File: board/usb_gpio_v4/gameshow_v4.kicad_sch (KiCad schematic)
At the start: 27 parts, among them J1 NC3FAAH, J2 NC3FAAH, J3 NC3FAAH, J4 NC3FAAH

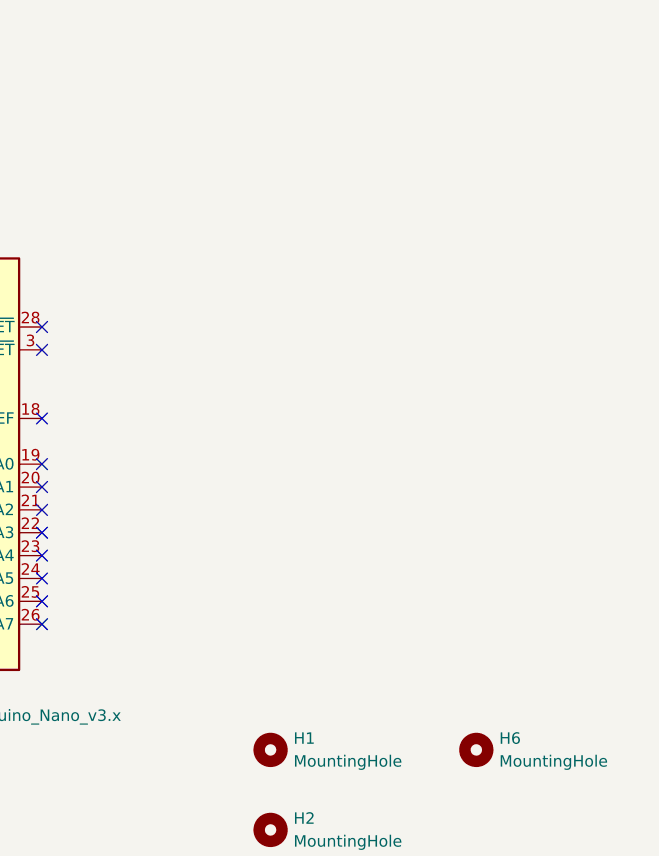
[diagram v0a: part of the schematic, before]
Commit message: add test switches
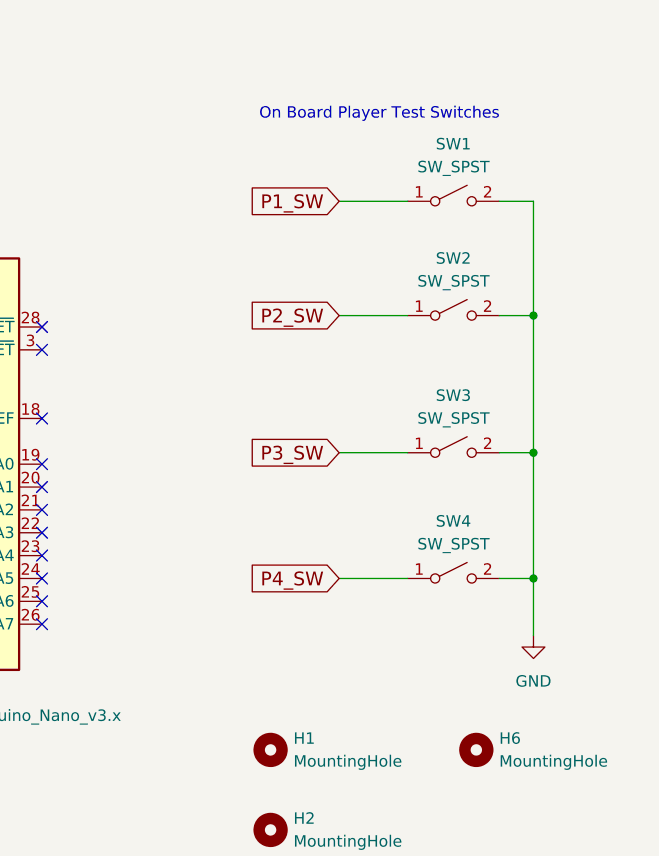
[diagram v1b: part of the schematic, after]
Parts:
- added SW1, SW2, SW3, SW4: SW_SPST, Button_Switch_SMD:SW_SPST_Omron_B3FS-101xP, symbol Switch:SW_SPST
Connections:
- net GND: now also SW1.2 (B), SW2.2 (B), SW3.2 (B), SW4.2 (B)
- net P1_SW: now also SW1.1 (A)
- net P2_SW: now also SW2.1 (A)
- net P3_SW: now also SW3.1 (A)
- net P4_SW: now also SW4.1 (A)
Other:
- note added: "On Board Player Test Switches"
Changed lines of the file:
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@@
   (junction (at 31.75 144.78) (diameter 0) (color 0 0 0 0)
   )
+  (junction (at 271.78 85.09) (diameter 0) (color 0 0 0 0)
+  )
+  (junction (at 271.78 99.06) (diameter 0) (color 0 0 0 0)
+  )
   (junction (at 127 45.72) (diameter 0) (color 0 0 0 0)
   )
@@
   )
   (junction (at 64.77 72.39) (diameter 0) (color 0 0 0 0)
+  )
+  (junction (at 271.78 69.85) (diameter 0) (color 0 0 0 0)
   )
   (junction (at 115.57 45.72) (diameter 0) (color 0 0 0 0)
@@
     (stroke (width 0) (type default))
   )
+  (wire (pts (xy 250.19 99.06) (xy 257.81 99.06))
+    (stroke (width 0) (type default))
+  )
   (wire (pts (xy 31.75 72.39) (xy 31.75 91.44))
     (stroke (width 0) (type default))
@@
     (stroke (width 0) (type default))
   )
+  (wire (pts (xy 271.78 99.06) (xy 271.78 85.09))
+    (stroke (width 0) (type default))
+  )
   (wire (pts (xy 207.01 118.11) (xy 204.47 118.11))
     (stroke (width 0) (type default))
@@
     (stroke (width 0) (type default))
   )
+  (wire (pts (xy 271.78 57.15) (xy 267.97 57.15))
+    (stroke (width 0) (type default))
+  )
   (wire (pts (xy 127 45.72) (xy 207.01 45.72))
     (stroke (width 0) (type default))
@@
     (stroke (width 0) (type default))
   )
+  (wire (pts (xy 267.97 85.09) (xy 271.78 85.09))
+    (stroke (width 0) (type default))
+  )
   (wire (pts (xy 31.75 144.78) (xy 31.75 158.75))
     (stroke (width 0) (type default))
@@
     (stroke (width 0) (type default))
   )
+  (wire (pts (xy 267.97 99.06) (xy 271.78 99.06))
+    (stroke (width 0) (type default))
+  )
   (wire (pts (xy 176.53 101.6) (xy 176.53 100.33))
     (stroke (width 0) (type default))
@@
     (stroke (width 0) (type default))
   )
+  (wire (pts (xy 271.78 85.09) (xy 271.78 69.85))
+    (stroke (width 0) (type default))
+  )
   (wire (pts (xy 69.85 102.87) (xy 63.5 102.87))
     (stroke (width 0) (type default))
@@
     (stroke (width 0) (type default))
   )
+  (wire (pts (xy 250.19 57.15) (xy 257.81 57.15))
+    (stroke (width 0) (type default))
+  )
   (wire (pts (xy 69.85 162.56) (xy 64.77 162.56))
     (stroke (width 0) (type default))
@@
     (stroke (width 0) (type default))
   )
+  (wire (pts (xy 271.78 69.85) (xy 271.78 57.15))
+    (stroke (width 0) (type default))
+  )
   (wire (pts (xy 31.75 158.75) (xy 31.75 179.07))
     (stroke (width 0) (type default))
@@
     (stroke (width 0) (type default))
   )
+  (wire (pts (xy 250.19 85.09) (xy 257.81 85.09))
+    (stroke (width 0) (type default))
+  )
+  (wire (pts (xy 271.78 105.41) (xy 271.78 99.06))
+    (stroke (width 0) (type default))
+  )
+  (wire (pts (xy 250.19 69.85) (xy 257.81 69.85))
+    (stroke (width 0) (type default))
+  )
   (wire (pts (xy 69.85 130.81) (xy 63.5 130.81))
     (stroke (width 0) (type default))
@@
     (stroke (width 0) (type default))
   )
+  (wire (pts (xy 267.97 69.85) (xy 271.78 69.85))
+    (stroke (width 0) (type default))
+  )
   (wire (pts (xy 167.64 86.36) (xy 191.77 86.36))
     (stroke (width 0) (type default))
@@
   (wire (pts (xy 48.26 91.44) (xy 43.18 91.44))
     (stroke (width 0) (type default))
+  )
+  (text "On Board Player Test Switches" (at 241.3 48.26 0)
+    (effects (font (size 1.27 1.27)) (justify left bottom))
   )
   (text "11/10/2023" (at 207.01 194.31 0)
@@
     )
   )
+  (global_label "P4_SW" (shape input) (at 250.19 99.06 180)
+    (effects (font (size 1.524 1.524)) (justify right))
+    (property "Intersheetrefs" "${INTERSHEET_REFS}" (at 250.19 99.06 0)
+      (effects (font (size 1.27 1.27)) hide)
+    )
+  )
   (global_label "P3_SW" (shape input) (at 173.99 96.52 180)
     (effects (font (size 1.524 1.524)) (justify right))
@@
     )
   )
+  (global_label "P2_SW" (shape input) (at 250.19 69.85 180)
+    (effects (font (size 1.524 1.524)) (justify right))
+    (property "Intersheetrefs" "${INTERSHEET_REFS}" (at 250.19 69.85 0)
+      (effects (font (size 1.27 1.27)) hide)
+    )
+  )
   (global_label "P4_SW" (shape output) (at 69.85 162.56 0)
     (effects (font (size 1.524 1.524)) (justify left))
@@
     )
   )
+  (global_label "P3_SW" (shape input) (at 250.19 85.09 180)
+    (effects (font (size 1.524 1.524)) (justify right))
+    (property "Intersheetrefs" "${INTERSHEET_REFS}" (at 250.19 85.09 0)
+      (effects (font (size 1.27 1.27)) hide)
+    )
+  )
   (global_label "P2_SW" (shape output) (at 69.85 102.87 0)
     (effects (font (size 1.524 1.524)) (justify left))
@@
     (effects (font (size 1.524 1.524)) (justify left))
     (property "Intersheetrefs" "${INTERSHEET_REFS}" (at 69.85 130.81 0)
+      (effects (font (size 1.27 1.27)) hide)
+    )
+  )
+  (global_label "P1_SW" (shape input) (at 250.19 57.15 180)
+    (effects (font (size 1.524 1.524)) (justify right))
+    (property "Intersheetrefs" "${INTERSHEET_REFS}" (at 250.19 57.15 0)
       (effects (font (size 1.27 1.27)) hide)
     )
@@
     )
   )
+  (symbol (lib_id "Switch:SW_SPST") (at 262.89 69.85 0) (unit 1)
+    (in_bom yes) (on_board yes) (dnp no) (fields_autoplaced)
+    (property "Reference" "SW2" (at 262.89 63.5 0)
+      (effects (font (size 1.27 1.27)))
+    )
+    (property "Value" "SW_SPST" (at 262.89 66.04 0)
+      (effects (font (size 1.27 1.27)))
+    )
+    (property "Footprint" "Button_Switch_SMD:SW_SPST_Omron_B3FS-101xP" (at 262.89 69.85 0)
+      (effects (font (size 1.27 1.27)) hide)
+    )
+    (property "Datasheet" "~" (at 262.89 69.85 0)
+      (effects (font (size 1.27 1.27)) hide)
+    )
+    (pin "1")
+    (pin "2")
+    (instances
+      (project "gameshow_v4"
+        (path "/8006f48b-a5c4-43ae-b413-2d00a40f6198"
+          (reference "SW2") (unit 1)
+        )
+      )
+    )
+  )
   (symbol (lib_id "power:PWR_FLAG") (at 204.47 121.92 90) (unit 1)
     (in_bom yes) (on_board yes) (dnp no) (fields_autoplaced)
@@
         (path "/8006f48b-a5c4-43ae-b413-2d00a40f6198"
           (reference "#FLG01") (unit 1)
+        )
+      )
+    )
+  )
+  (symbol (lib_id "Switch:SW_SPST") (at 262.89 57.15 0) (unit 1)
+    (in_bom yes) (on_board yes) (dnp no) (fields_autoplaced)
+    (property "Reference" "SW1" (at 262.89 50.8 0)
+      (effects (font (size 1.27 1.27)))
+    )
+    (property "Value" "SW_SPST" (at 262.89 53.34 0)
+      (effects (font (size 1.27 1.27)))
+    )
+    (property "Footprint" "Button_Switch_SMD:SW_SPST_Omron_B3FS-101xP" (at 262.89 57.15 0)
+      (effects (font (size 1.27 1.27)) hide)
+    )
+    (property "Datasheet" "~" (at 262.89 57.15 0)
+      (effects (font (size 1.27 1.27)) hide)
+    )
+    (pin "1")
+    (pin "2")
+    (instances
+      (project "gameshow_v4"
+        (path "/8006f48b-a5c4-43ae-b413-2d00a40f6198"
+          (reference "SW1") (unit 1)
         )
       )
@@
     )
   )
+  (symbol (lib_id "power:GND") (at 271.78 105.41 0) (unit 1)
+    (in_bom yes) (on_board yes) (dnp no) (fields_autoplaced)
+    (property "Reference" "#PWR03" (at 271.78 111.76 0)
+      (effects (font (size 1.27 1.27)) hide)
+    )
+    (property "Value" "GND" (at 271.78 110.49 0)
+      (effects (font (size 1.27 1.27)))
+    )
+    (property "Footprint" "" (at 271.78 105.41 0)
+      (effects (font (size 1.27 1.27)) hide)
+    )
+    (property "Datasheet" "" (at 271.78 105.41 0)
+      (effects (font (size 1.27 1.27)) hide)
+    )
+    (pin "1")
+    (instances
+      (project "gameshow_v4"
+        (path "/8006f48b-a5c4-43ae-b413-2d00a40f6198"
+          (reference "#PWR03") (unit 1)
+        )
+      )
+    )
+  )
   (symbol (lib_id "Device:LED") (at 39.37 91.44 0) (unit 1)
     (in_bom yes) (on_board yes) (dnp no) (fields_autoplaced)
@@
     )
   )
+  (symbol (lib_id "Switch:SW_SPST") (at 262.89 99.06 0) (unit 1)
+    (in_bom yes) (on_board yes) (dnp no) (fields_autoplaced)
+    (property "Reference" "SW4" (at 262.89 92.71 0)
+      (effects (font (size 1.27 1.27)))
+    )
+    (property "Value" "SW_SPST" (at 262.89 95.25 0)
+      (effects (font (size 1.27 1.27)))
+    )
+    (property "Footprint" "Button_Switch_SMD:SW_SPST_Omron_B3FS-101xP" (at 262.89 99.06 0)
+      (effects (font (size 1.27 1.27)) hide)
+    )
+    (property "Datasheet" "~" (at 262.89 99.06 0)
+      (effects (font (size 1.27 1.27)) hide)
+    )
+    (property "Field4" "" (at 262.89 99.06 0)
+      (effects (font (size 1.27 1.27)) hide)
+    )
+    (pin "1")
+    (pin "2")
+    (instances
+      (project "gameshow_v4"
+        (path "/8006f48b-a5c4-43ae-b413-2d00a40f6198"
+          (reference "SW4") (unit 1)
+        )
+      )
+    )
+  )
   (symbol (lib_id "Device:R") (at 115.57 54.61 0) (unit 1)
     (in_bom yes) (on_board yes) (dnp no) (fields_autoplaced)
@@
         )
       )
+    )
+  )
+  (symbol (lib_id "Switch:SW_SPST") (at 262.89 85.09 0) (unit 1)
+    (in_bom yes) (on_board yes) (dnp no) (fields_autoplaced)
+    (property "Reference" "SW3" (at 262.89 78.74 0)
+      (effects (font (size 1.27 1.27)))
+    )
+    (property "Value" "SW_SPST" (at 262.89 81.28 0)
+      (effects (font (size 1.27 1.27)))
+    )
+    (property "Footprint" "Button_Switch_SMD:SW_SPST_Omron_B3FS-101xP" (at 262.89 85.09 0)
+      (effects (font (size 1.27 1.27)) hide)
+    )
+    (property "Datasheet" "~" (at 262.89 85.09 0)
+      (effects (font (size 1.27 1.27)) hide)
+    )
+    (pin "1")
+    (pin "2")
+    (instances
+      (project "gameshow_v4"
+        (path "/8006f48b-a5c4-43ae-b413-2d00a40f6198"
+          (reference "SW3") (unit 1)
+        )
+      )

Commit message: refactor code
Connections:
- no-connect marks 18 -> 19
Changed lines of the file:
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@@
   (no_connect (at 191.77 76.2))
   (no_connect (at 217.17 96.52))
+  (no_connect (at 191.77 91.44))
   (no_connect (at 217.17 86.36))
   (no_connect (at 191.77 78.74))
